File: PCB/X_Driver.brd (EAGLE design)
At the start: 131.6 x 117.6 mm, 55 parts, among them IC1 A4982, IC2 A4982, IC3 FT232RL, IC4 7805DT, Q1 20MHz, U1 ATMEGA168, X1 USBSMD, X1_ENC OPB990P51, X1_MOTOR X_STEPPER, X1_P yellow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

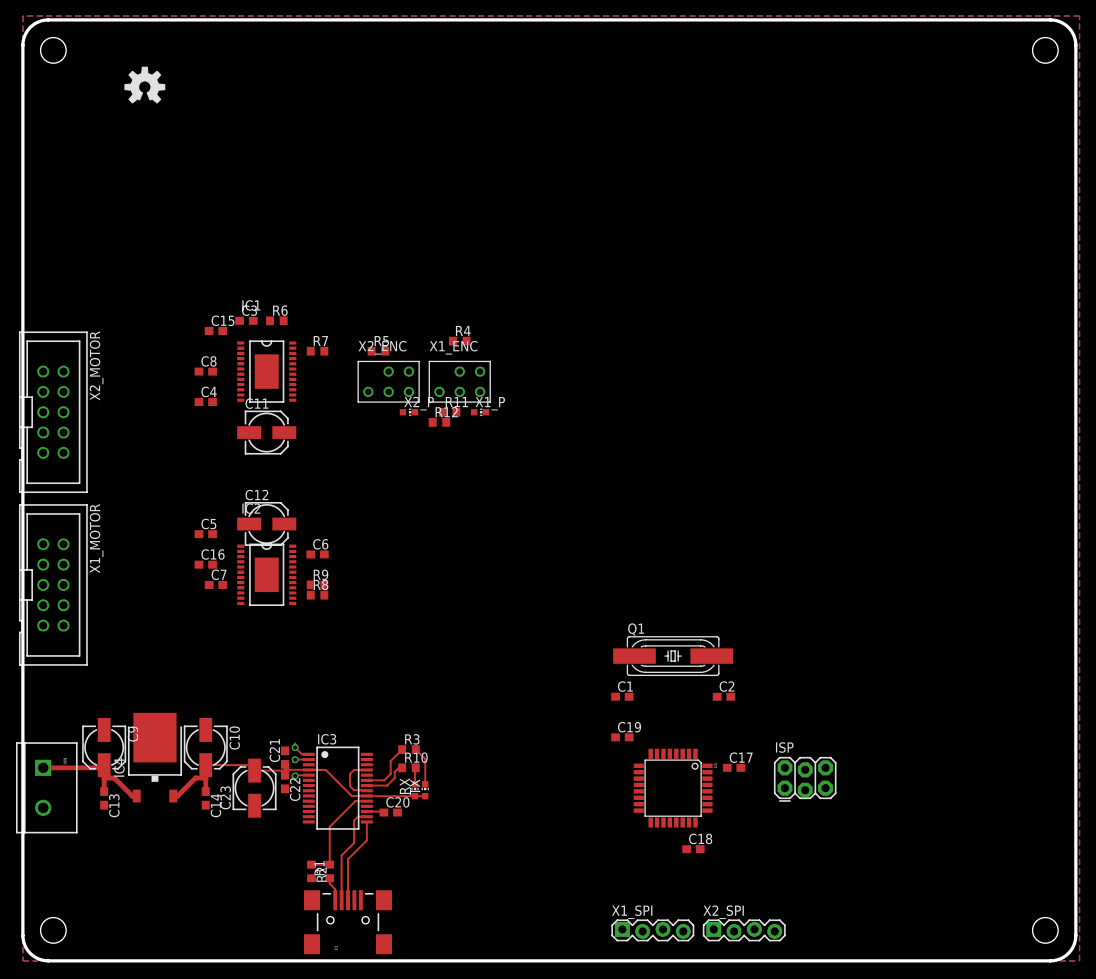
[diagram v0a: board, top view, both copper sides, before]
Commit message: Routed X driver, both boards need DRC.
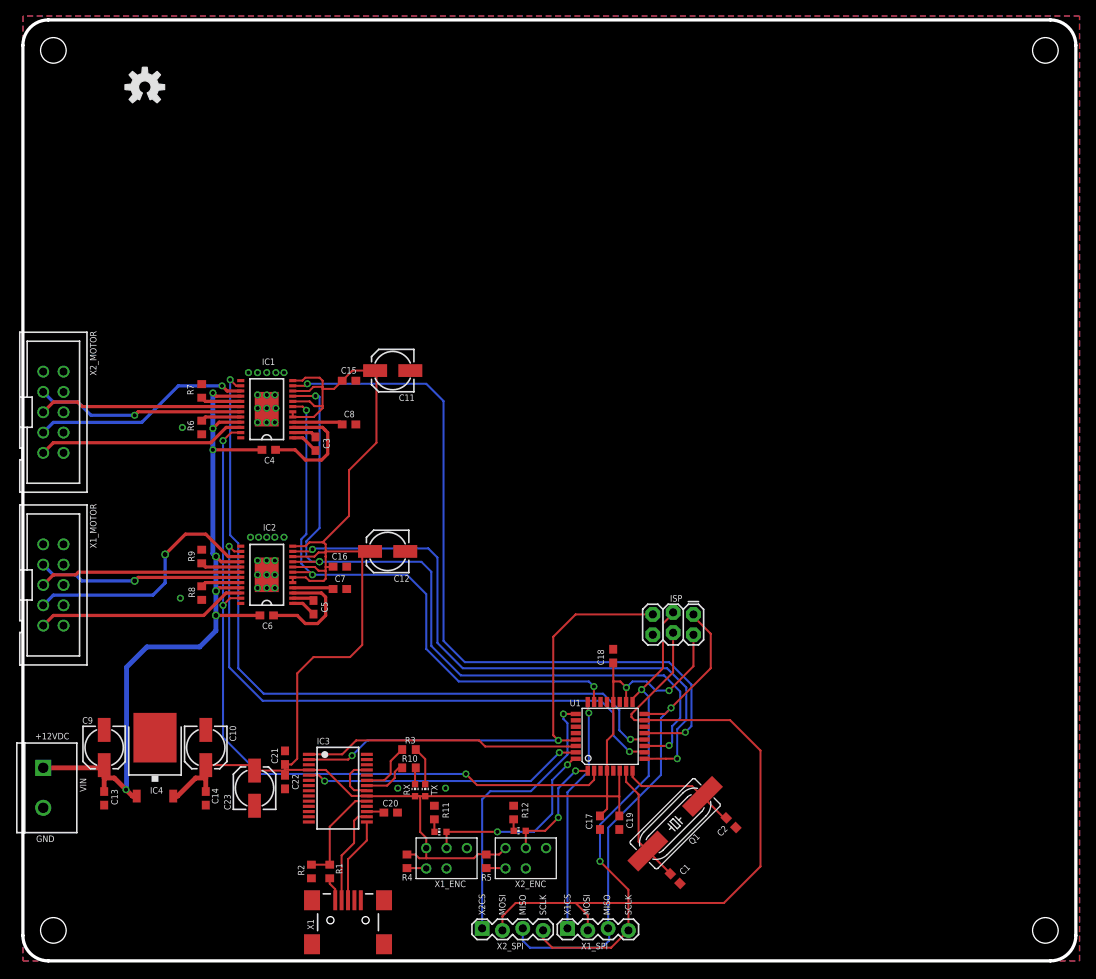
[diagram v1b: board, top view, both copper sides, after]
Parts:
- moved R4 65.4 mm to (48.0, 12.4), turned to 270 degrees
- moved R5 65.2 mm to (57.9, 12.4), turned to 270 degrees
- moved X2_ENC 62.0 mm to (62.9, 12.8), turned to 180 degrees
- moved X1_ENC 59.6 mm to (53.0, 12.8), turned to 180 degrees
- moved X2_P 54.1 mm to (62.1, 16.3), turned to 90 degrees
- moved X1_P 52.7 mm to (52.2, 16.1), turned to 90 degrees
- moved R11 50.1 mm to (51.4, 18.5), turned to 270 degrees
- moved R12 49.6 mm to (61.3, 18.5), turned to 270 degrees
- moved X2_SPI 29.0 mm to (57.4, 3.94)
- moved C18 26.1 mm to (73.8, 38.1), turned to 90 degrees
- moved ISP 24.5 mm to (83.8, 43.3), turned to 180 degrees
- moved C1 23.7 mm to (81.5, 10.3), turned to 315 degrees
- moved Q1 21.0 mm to (81.5, 17.1), turned to 225 degrees
- moved C8 19.1 mm to (40.8, 67.1)
- moved C17 18.1 mm to (72.1, 17.3), turned to 270 degrees
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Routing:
- net VCC: track 38.8 -> 242.8 mm, vias 0 -> 2
- net MSLP: track 0.00 -> 97.0 mm, vias 0 -> 4
- net X2STP: track 0.00 -> 94.5 mm, vias 0 -> 2
- net X2DIR: track 0.00 -> 94.2 mm, vias 0 -> 2
- net MEN: track 0.00 -> 92.6 mm, vias 0 -> 3
- net MOSI: track 0.00 -> 85.8 mm
- net 12VDC: track 15.9 -> 99.9 mm, vias 0 -> 7
- net X1STP: track 0.00 -> 76.3 mm, vias 0 -> 2
- net X1DIR: track 0.00 -> 74.8 mm, vias 0 -> 2
- net MRST: track 0.00 -> 72.8 mm, vias 0 -> 3
- net MISO: track 0.00 -> 63.7 mm, vias 0 -> 1
- net SCK: track 0.00 -> 60.8 mm, vias 0 -> 2
- net RESET: track 1.97 -> 61.2 mm, vias 1 -> 2
- net X2CS: track 0.00 -> 36.0 mm, vias 0 -> 1
- net TX: track 2.26 -> 35.2 mm, vias 1 -> 2
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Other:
- board text added: "+12VDC"
- board text added: "GND"
- board text added: "MISO"
- board text added: "MOSI"
- board text added: "SCLK"
- board text added: "X1CS"
- board text added: "X2CS"
